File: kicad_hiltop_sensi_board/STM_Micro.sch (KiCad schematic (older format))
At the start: 20 parts, among them SW1 SW_Push, U22 STM32F072RBTx, Y2 8MHZ, Y3 ABS25-32.768KHZ-6-T

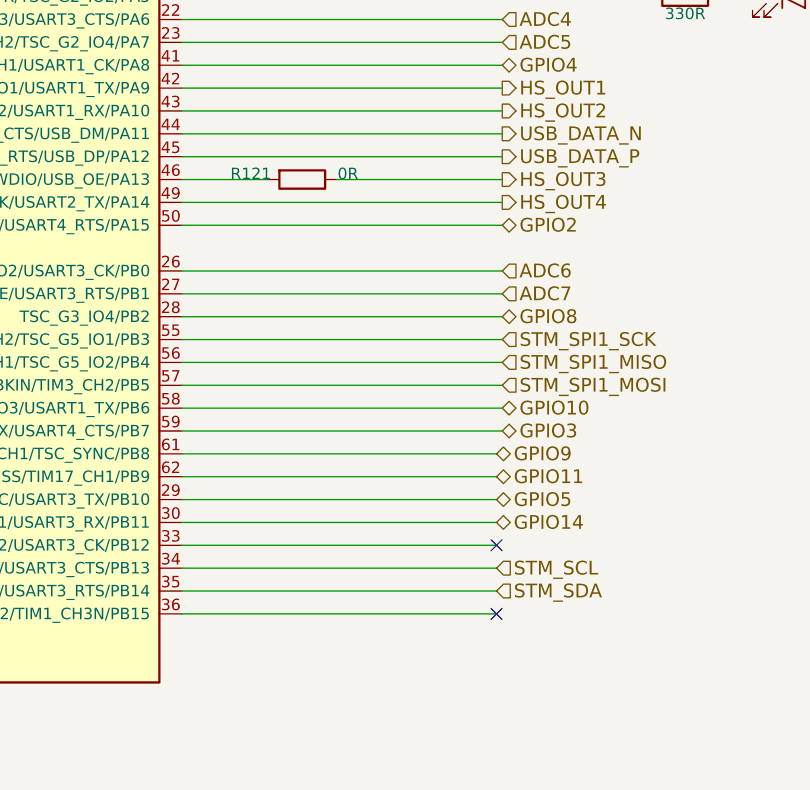
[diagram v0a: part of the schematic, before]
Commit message: Started on Sensi Board Layout
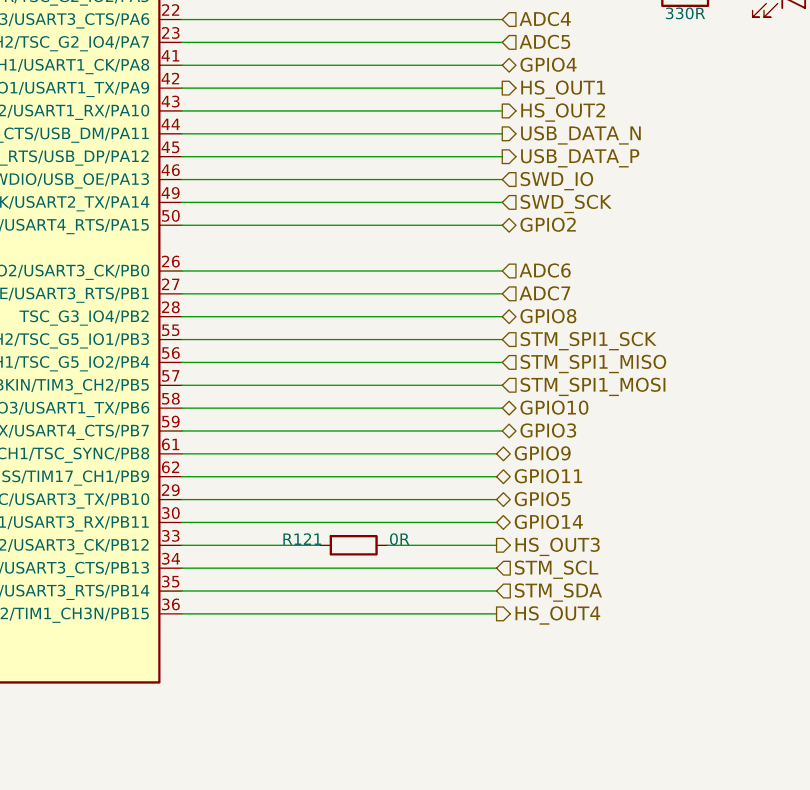
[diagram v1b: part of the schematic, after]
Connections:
- net HS_OUT4: now also U22.36 (I2S2_SD/RTC_REFIN/SPI2_MOSI/SYS_WKUP7/TIM15_CH1N/TIM15_CH2/TIM1_CH3N/PB15); no longer U22.49 (SYS_SWCLK/USART2_TX/PA14)
- net at U22.33 (I2S2_WS/SPI2_NSS/TIM15_BKIN/TIM1_BKIN/TSC_G6_IO2/USART3_CK/PB12): now also R121.2
- net SWD_IO: now reaches U22.46 (IR_OUT/SYS_SWDIO/USB_OE/PA13)
- net SWD_IO: no longer R121.2
- new net SWD_SCK: U22.49 (SYS_SWCLK/USART2_TX/PA14)
- no-connect marks 8 -> 6
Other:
- moved on the sheet: R121
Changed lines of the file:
@@
 	4400 5575 3925 5575
-Wire Wire Line
-	10400 5975 11775 5975
 Wire Wire Line
 	10400 5875 11775 5875
@@
 L Sensi_Board-rescue:R-device R121
 U 1 1 5FA9D488
-P 10925 4375
-F 0 "R121" V 10900 4150 50  0000 C CNN
-F 1 "0R" V 10900 4575 50  0000 C CNN
-F 2 "Resistor_SMD:R_0603_1608Metric" V 10855 4375 50  0001 C CNN
-F 3 "" H 10925 4375 50  0001 C CNN
-F 4 "101-005" H 0   0   50  0001 C CNN "Devtank"
-	1    10925 4375
+P 11150 5975
+F 0 "R121" V 11125 5750 50  0000 C CNN
+F 1 "0R" V 11125 6175 50  0000 C CNN
+F 2 "Resistor_SMD:R_0603_1608Metric" V 11080 5975 50  0001 C CNN
+F 3 "" H 11150 5975 50  0001 C CNN
+F 4 "101-005" H 225 1600 50  0001 C CNN "Devtank"
+	1    11150 5975
 	0    1    1    0
 $EndComp
-Wire Wire Line
-	10775 4375 10400 4375
-Wire Wire Line
-	11075 4375 11800 4375
-Wire Wire Line
-	10400 4475 11800 4475
 Text HLabel 11800 3975 2    60   Output ~ 0
 HS_OUT1
 Text HLabel 11800 4075 2    60   Output ~ 0
 HS_OUT2
-Text HLabel 11800 4375 2    60   Output ~ 0
+Text HLabel 11775 5975 2    60   Output ~ 0
 HS_OUT3
-Text HLabel 11800 4475 2    60   Output ~ 0
+Text HLabel 11775 6275 2    60   Output ~ 0
 HS_OUT4
 Text HLabel 11800 3075 2    60   Input ~ 0
@@
 Text HLabel 11775 6175 2    60   Input ~ 0
 STM_SDA
-NoConn ~ 11775 5975
-NoConn ~ 11775 6275
 NoConn ~ 4400 5375
 NoConn ~ 4400 3475
@@
 Text HLabel 11800 3675 2    60   Input ~ 0
 ADC4
+Wire Wire Line
+	10400 4475 11800 4475
+Wire Wire Line
+	10400 4375 11800 4375
+Text HLabel 11800 4375 2    60   Input ~ 0
+SWD_IO
+Text HLabel 11800 4475 2    60   Input ~ 0
+SWD_SCK
+Wire Wire Line
+	11300 5975 11775 5975
+Wire Wire Line
+	11000 5975 10400 5975
 $EndSCHEMATC

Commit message: Updated sensi board layout LBBC
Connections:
- net ADC1: now also U22.11 (PC3/ADC_IN13/I2S2_SD/SPI2_MOSI); no longer U22.14 (ADC_IN0/COMP1_INM/COMP1_OUT/RTC_TAMP2/SYS_WKUP1/TIM2_CH1/TIM2_ETR/TSC_G1_IO1/USART2_CTS/USART4_TX/PA0)
- net ADC10: now also U22.22 (ADC_IN6/COMP1_OUT/I2S1_MCK/SPI1_MISO/TIM16_CH1/TIM1_BKIN/TIM3_CH1/TSC_G2_IO3/USART3_CTS/PA6); no longer U22.10 (PC2/ADC_IN12/I2S2_MCK/SPI2_MISO)
- net ADC11: now also U22.23 (ADC_IN7/COMP2_OUT/I2S1_SD/SPI1_MOSI/TIM14_CH1/TIM17_CH1/TIM1_CH1N/TIM3_CH2/TSC_G2_IO4/PA7); no longer U22.11 (PC3/ADC_IN13/I2S2_SD/SPI2_MOSI)
- net ADC2: now also U22.10 (PC2/ADC_IN12/I2S2_MCK/SPI2_MISO); no longer U22.15 (ADC_IN1/COMP1_INP/TIM15_CH1N/TIM2_CH2/TSC_G1_IO2/USART2_DE/USART2_RTS/USART4_RX/PA1)
- net ADC3: now also U22.9 (PC1/ADC_IN11); no longer U22.20 (ADC_IN4/COMP1_INM/COMP2_INM/DAC_OUT1/I2S1_WS/SPI1_NSS/TIM14_CH1/TSC_G2_IO1/USART2_CK/PA4)
- net ADC4: now also U22.8 (PC0/ADC_IN10); no longer U22.22 (ADC_IN6/COMP1_OUT/I2S1_MCK/SPI1_MISO/TIM16_CH1/TIM1_BKIN/TIM3_CH1/TSC_G2_IO3/USART3_CTS/PA6)
- net ADC5: now also U22.14 (ADC_IN0/COMP1_INM/COMP1_OUT/RTC_TAMP2/SYS_WKUP1/TIM2_CH1/TIM2_ETR/TSC_G1_IO1/USART2_CTS/USART4_TX/PA0); no longer U22.23 (ADC_IN7/COMP2_OUT/I2S1_SD/SPI1_MOSI/TIM14_CH1/TIM17_CH1/TIM1_CH1N/TIM3_CH2/TSC_G2_IO4/PA7)
- net ADC6: now also U22.15 (ADC_IN1/COMP1_INP/TIM15_CH1N/TIM2_CH2/TSC_G1_IO2/USART2_DE/USART2_RTS/USART4_RX/PA1); no longer U22.26 (ADC_IN8/TIM1_CH2N/TIM3_CH3/TSC_G3_IO2/USART3_CK/PB0)
- net ADC7: now also U22.16 (ADC_IN2/COMP2_INM/COMP2_OUT/SYS_WKUP4/TIM15_CH1/TIM2_CH3/TSC_G1_IO3/USART2_TX/PA2); no longer U22.27 (ADC_IN9/TIM14_CH1/TIM1_CH3N/TIM3_CH4/TSC_G3_IO3/USART3_DE/USART3_RTS/PB1)
- net ADC8: now also U22.17 (ADC_IN3/COMP2_INP/TIM15_CH2/TIM2_CH4/TSC_G1_IO4/USART2_RX/PA3); no longer U22.8 (PC0/ADC_IN10)
- net ADC9: now also U22.20 (ADC_IN4/COMP1_INM/COMP2_INM/DAC_OUT1/I2S1_WS/SPI1_NSS/TIM14_CH1/TSC_G2_IO1/USART2_CK/PA4); no longer U22.9 (PC1/ADC_IN11)
- net DEBUG_UART_RX: now also U22.30 (I2C2_SDA/TIM2_CH4/TSC_G6_IO1/USART3_RX/PB11); no longer U22.17 (ADC_IN3/COMP2_INP/TIM15_CH2/TIM2_CH4/TSC_G1_IO4/USART2_RX/PA3)
- net DEBUG_UART_TX: now also U22.29 (CEC/I2C2_SCL/I2S2_CK/SPI2_SCK/TIM2_CH3/TSC_SYNC/USART3_TX/PB10); no longer U22.16 (ADC_IN2/COMP2_INM/COMP2_OUT/SYS_WKUP4/TIM15_CH1/TIM2_CH3/TSC_G1_IO3/USART2_TX/PA2)
- net DUT1_UART_RX_GPIO15: now also U22.52 (PC11/USART3_RX/USART4_RX); no longer U22.51 (PC10/USART3_TX/USART4_TX)
- net DUT1_UART_TX_GPIO16: now also U22.53 (PC12/USART3_CK/USART4_CK); no longer U22.52 (PC11/USART3_RX/USART4_RX)
- net GPIO1: now also U22.39 (PC8/TIM3_CH3); no longer U22.53 (PC12/USART3_CK/USART4_CK)
- net GPIO10: now also U22.62 (CAN_TX/DAC_EXTI9/I2C1_SDA/I2S2_WS/IR_OUT/SPI2_NSS/TIM17_CH1/PB9); no longer U22.58 (I2C1_SCL/TIM16_CH1N/TSC_G5_IO3/USART1_TX/PB6)
- net GPIO11: now also U22.2 (PC13/RTC_OUT_ALARM/RTC_OUT_CALIB/RTC_TAMP1/RTC_TS/SYS_WKUP2); no longer U22.62 (CAN_TX/DAC_EXTI9/I2C1_SDA/I2S2_WS/IR_OUT/SPI2_NSS/TIM17_CH1/PB9)
- net GPIO12: now also U22.27 (ADC_IN9/TIM14_CH1/TIM1_CH3N/TIM3_CH4/TSC_G3_IO3/USART3_DE/USART3_RTS/PB1); no longer U22.38 (PC7/TIM3_CH2)
- net GPIO14: now also U22.26 (ADC_IN8/TIM1_CH2N/TIM3_CH3/TSC_G3_IO2/USART3_CK/PB0); no longer U22.30 (I2C2_SDA/TIM2_CH4/TSC_G6_IO1/USART3_RX/PB11)
- net GPIO2: now also U22.41 (CRS_SYNC/RCC_MCO/TIM1_CH1/USART1_CK/PA8); no longer U22.50 (I2S1_WS/SPI1_NSS/TIM2_CH1/TIM2_ETR/USART2_RX/USART4_DE/USART4_RTS/PA15)
- net GPIO3: now also U22.28 (TSC_G3_IO4/PB2); no longer U22.59 (I2C1_SDA/TIM17_CH1N/TSC_G5_IO4/USART1_RX/USART4_CTS/PB7)
- net GPIO4: now also U22.42 (DAC_EXTI9/TIM15_BKIN/TIM1_CH2/TSC_G4_IO1/USART1_TX/PA9); no longer U22.41 (CRS_SYNC/RCC_MCO/TIM1_CH1/USART1_CK/PA8)
- net GPIO5: now also U22.34 (I2C2_SCL/I2S2_CK/SPI2_SCK/TIM1_CH1N/TSC_G6_IO3/USART3_CTS/PB13); no longer U22.29 (CEC/I2C2_SCL/I2S2_CK/SPI2_SCK/TIM2_CH3/TSC_SYNC/USART3_TX/PB10)
- net GPIO6: now also U22.35 (I2C2_SDA/I2S2_MCK/SPI2_MISO/TIM15_CH1/TIM1_CH2N/TSC_G6_IO4/USART3_DE/USART3_RTS/PB14); no longer U22.2 (PC13/RTC_OUT_ALARM/RTC_OUT_CALIB/RTC_TAMP1/RTC_TS/SYS_WKUP2)
- net GPIO7: now also U22.36 (I2S2_SD/RTC_REFIN/SPI2_MOSI/SYS_WKUP7/TIM15_CH1N/TIM15_CH2/TIM1_CH3N/PB15); no longer U22.54 (PD2/TIM3_ETR/USART3_DE/USART3_RTS)
- net GPIO8: now also U22.38 (PC7/TIM3_CH2); no longer U22.28 (TSC_G3_IO4/PB2)
- net HS_OUT1: now also U22.43 (TIM17_BKIN/TIM1_CH3/TSC_G4_IO2/USART1_RX/PA10); no longer U22.42 (DAC_EXTI9/TIM15_BKIN/TIM1_CH2/TSC_G4_IO1/USART1_TX/PA9)
- net HS_OUT2: now also U22.33 (I2S2_WS/SPI2_NSS/TIM15_BKIN/TIM1_BKIN/TSC_G6_IO2/USART3_CK/PB12); no longer U22.43 (TIM17_BKIN/TIM1_CH3/TSC_G4_IO2/USART1_RX/PA10)
- net HS_OUT4: now also U22.50 (I2S1_WS/SPI1_NSS/TIM2_CH1/TIM2_ETR/USART2_RX/USART4_DE/USART4_RTS/PA15); no longer U22.36 (I2S2_SD/RTC_REFIN/SPI2_MOSI/SYS_WKUP7/TIM15_CH1N/TIM15_CH2/TIM1_CH3N/PB15)
- net RL1: now also U22.54 (PD2/TIM3_ETR/USART3_DE/USART3_RTS); no longer U22.39 (PC8/TIM3_CH3)
- net STM_SCL: now also U22.58 (I2C1_SCL/TIM16_CH1N/TSC_G5_IO3/USART1_TX/PB6); no longer U22.34 (I2C2_SCL/I2S2_CK/SPI2_SCK/TIM1_CH1N/TSC_G6_IO3/USART3_CTS/PB13)
- net STM_SDA: now also U22.59 (I2C1_SDA/TIM17_CH1N/TSC_G5_IO4/USART1_RX/USART4_CTS/PB7); no longer U22.35 (I2C2_SDA/I2S2_MCK/SPI2_MISO/TIM15_CH1/TIM1_CH2N/TSC_G6_IO4/USART3_DE/USART3_RTS/PB14)
- net at R121.2: now also U22.51 (PC10/USART3_TX/USART4_TX); no longer U22.33 (I2S2_WS/SPI2_NSS/TIM15_BKIN/TIM1_BKIN/TSC_G6_IO2/USART3_CK/PB12)
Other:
- moved on the sheet: R121
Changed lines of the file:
@@
 	4400 5075 3925 5075
 Wire Wire Line
-	4400 5975 3925 5975
-Wire Wire Line
 	10400 4575 11800 4575
 Wire Wire Line
@@
 Wire Wire Line
 	10400 4075 11800 4075
-$Comp
-L Sensi_Board-rescue:R-device R121
-U 1 1 5FA9D488
-P 11150 5975
-F 0 "R121" V 11125 5750 50  0000 C CNN
-F 1 "0R" V 11125 6175 50  0000 C CNN
-F 2 "Resistor_SMD:R_0603_1608Metric" V 11080 5975 50  0001 C CNN
-F 3 "" H 11150 5975 50  0001 C CNN
-F 4 "101-005" H 225 1600 50  0001 C CNN "Devtank"
-	1    11150 5975
-	0    1    1    0
-$EndComp
-Text HLabel 11800 3975 2    60   Output ~ 0
+Text HLabel 11800 4075 2    60   Output ~ 0
 HS_OUT1
-Text HLabel 11800 4075 2    60   Output ~ 0
-HS_OUT2
-Text HLabel 11775 5975 2    60   Output ~ 0
-HS_OUT3
-Text HLabel 11775 6275 2    60   Output ~ 0
+Text HLabel 11800 4575 2    60   Output ~ 0
 HS_OUT4
-Text HLabel 11800 3075 2    60   Input ~ 0
-ADC1
-Text HLabel 11800 3175 2    60   Input ~ 0
-ADC2
-Text HLabel 11800 3375 2    60   Input ~ 0
-DEBUG_UART_RX
-Text HLabel 11800 3275 2    60   Output ~ 0
+Text HLabel 11775 5775 2    60   Output ~ 0
 DEBUG_UART_TX
-Text HLabel 11800 3475 2    60   Input ~ 0
+Text HLabel 3925 4875 0    60   Input ~ 0
 ADC3
 $Comp
@@
 Wire Wire Line
 	13325 3575 13225 3575
-Text HLabel 11800 3775 2    60   Input ~ 0
-ADC5
-Text HLabel 11800 3875 2    60   BiDi ~ 0
+Text HLabel 11800 3975 2    60   BiDi ~ 0
 GPIO4
 Text HLabel 11800 4175 2    60   Output ~ 0
@@
 Text HLabel 11800 4275 2    60   Output ~ 0
 USB_DATA_P
-Text HLabel 11800 4575 2    60   BiDi ~ 0
+Text HLabel 11800 3875 2    60   BiDi ~ 0
 GPIO2
-Text HLabel 11800 4875 2    60   Input ~ 0
+Text HLabel 11800 3275 2    60   Input ~ 0
 ADC7
 Text HLabel 4400 5675 0    60   BiDi ~ 0
 GPIO13
-Text HLabel 4400 6075 0    60   BiDi ~ 0
-GPIO6
-Text HLabel 11800 5375 2    60   BiDi ~ 0
+Text HLabel 11775 5675 2    60   BiDi ~ 0
 GPIO10
-Text HLabel 11800 5475 2    60   BiDi ~ 0
-GPIO3
-Text HLabel 11775 5775 2    60   BiDi ~ 0
+Text HLabel 11775 6075 2    60   BiDi ~ 0
 GPIO5
 Text HLabel 11775 5575 2    60   BiDi ~ 0
 GPIO9
-Text HLabel 11775 5675 2    60   BiDi ~ 0
+Text HLabel 4400 6075 0    60   BiDi ~ 0
 GPIO11
-Text HLabel 11775 5875 2    60   BiDi ~ 0
+Text HLabel 11800 4775 2    60   BiDi ~ 0
 GPIO14
-Text HLabel 3925 4575 0    60   BiDi ~ 0
+Text HLabel 11775 6275 2    60   BiDi ~ 0
 GPIO7
-Text HLabel 3925 4775 0    60   Input ~ 0
-ADC8
-Text HLabel 3925 4875 0    60   Input ~ 0
-ADC9
-Text HLabel 3925 5075 0    60   Input ~ 0
-ADC11
 Text HLabel 3925 5175 0    60   Input ~ 0
 ADC12
 Text HLabel 3925 5275 0    60   Input ~ 0
 ADC13
-Text HLabel 3925 5475 0    60   BiDi ~ 0
+Text HLabel 11800 4875 2    60   BiDi ~ 0
 GPIO12
-Text HLabel 3925 5575 0    60   Output ~ 0
+Text HLabel 3925 4575 0    60   Output ~ 0
 RL1
-Text HLabel 2200 5775 0    60   BiDi ~ 0
+Text HLabel 2500 5875 0    60   BiDi ~ 0
 DUT1_UART_RX_GPIO15
-Text HLabel 3925 5975 0    60   Input ~ 0
+Text HLabel 3925 5575 0    60   Input ~ 0
 GPIO1
-Text HLabel 11800 4775 2    60   Input ~ 0
+Text HLabel 11800 3175 2    60   Input ~ 0
 ADC6
 Wire Wire Line
@@
 Wire Wire Line
 	10400 3175 11800 3175
-Text HLabel 2200 5875 0    60   BiDi ~ 0
+Text HLabel 2500 5975 0    60   BiDi ~ 0
 DUT1_UART_TX_GPIO16
-Wire Wire Line
-	2200 5775 4400 5775
-Wire Wire Line
-	2200 5875 4400 5875
-Text HLabel 11800 4975 2    60   BiDi ~ 0
+Text HLabel 3925 5475 0    60   BiDi ~ 0
 GPIO8
-Text HLabel 3925 4975 0    60   Input ~ 0
-ADC10
 Wire Wire Line
 	2125 3275 4400 3275
@@
 Text HLabel 11800 5275 2    60   Input ~ 0
 STM_SPI1_MOSI
-Text HLabel 11775 6075 2    60   Input ~ 0
+Text HLabel 11800 5375 2    60   Input ~ 0
 STM_SCL
-Text HLabel 11775 6175 2    60   Input ~ 0
+Text HLabel 11800 5475 2    60   Input ~ 0
 STM_SDA
 NoConn ~ 4400 5375
@@
 NoConn ~ 3425 6550
 NoConn ~ 3025 6550
-Text HLabel 11800 3675 2    60   Input ~ 0
-ADC4
 Wire Wire Line
 	10400 4475 11800 4475
@@
 Text HLabel 11800 4475 2    60   Input ~ 0
 SWD_SCK
-Wire Wire Line
-	11300 5975 11775 5975
-Wire Wire Line
-	11000 5975 10400 5975
+Text HLabel 11800 3475 2    60   Input ~ 0
+ADC9
+Text HLabel 11800 3375 2    60   Input ~ 0
+ADC8
+Text HLabel 3925 4775 0    60   Input ~ 0
+ADC4
+Text HLabel 11800 3075 2    60   Input ~ 0
+ADC5
+Text HLabel 3925 4975 0    60   Input ~ 0
+ADC2
+Text HLabel 3925 5075 0    60   Input ~ 0
+ADC1
+Text HLabel 11800 5975 2    60   Output ~ 0
+HS_OUT2
+Text HLabel 11800 4975 2    60   BiDi ~ 0
+GPIO3
+Text HLabel 11775 6175 2    60   BiDi ~ 0
+GPIO6
+Wire Wire Line
+	3800 5775 4400 5775
+Wire Wire Line
+	3500 5775 3025 5775
+Text HLabel 11775 5875 2    60   Input ~ 0
+DEBUG_UART_RX
+Text HLabel 3025 5775 0    60   Output ~ 0
+HS_OUT3
+$Comp
+L Sensi_Board-rescue:R-device R121
+U 1 1 5FA9D488
+P 3650 5775
+F 0 "R121" V 3625 5550 50  0000 C CNN
+F 1 "0R" V 3625 5975 50  0000 C CNN
+F 2 "Resistor_SMD:R_0603_1608Metric" V 3580 5775 50  0001 C CNN
+F 3 "" H 3650 5775 50  0001 C CNN
+F 4 "101-005" H -7275 1400 50  0001 C CNN "Devtank"
+	1    3650 5775
+	0    -1   1    0
+$EndComp
+Wire Wire Line
+	2500 5875 4400 5875
+Wire Wire Line
+	4400 5975 2500 5975
+Wire Wire Line
+	10400 5975 11800 5975
+Text HLabel 11800 3675 2    60   Input ~ 0
+ADC10
+Text HLabel 11800 3775 2    60   Input ~ 0
+ADC11
 $EndSCHEMATC

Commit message: Sensi board updated pin map
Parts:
- C73, C74, C79, C80: footprint Capacitor_SMD:C_0603_1608Metric -> Capacitor_SMD:C_0402_1005Metric
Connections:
- net ADC1: now also U22.14 (ADC_IN0/COMP1_INM/COMP1_OUT/RTC_TAMP2/SYS_WKUP1/TIM2_CH1/TIM2_ETR/TSC_G1_IO1/USART2_CTS/USART4_TX/PA0); no longer U22.11 (PC3/ADC_IN13/I2S2_SD/SPI2_MOSI)
- net ADC10: now also U22.25 (PC5/ADC_IN15/SYS_WKUP5/TSC_G3_IO1/USART3_RX); no longer U22.22 (ADC_IN6/COMP1_OUT/I2S1_MCK/SPI1_MISO/TIM16_CH1/TIM1_BKIN/TIM3_CH1/TSC_G2_IO3/USART3_CTS/PA6)
- net ADC11: now also U22.24 (PC4/ADC_IN14/USART3_TX); no longer U22.23 (ADC_IN7/COMP2_OUT/I2S1_SD/SPI1_MOSI/TIM14_CH1/TIM17_CH1/TIM1_CH1N/TIM3_CH2/TSC_G2_IO4/PA7)
- net ADC12: now also U22.23 (ADC_IN7/COMP2_OUT/I2S1_SD/SPI1_MOSI/TIM14_CH1/TIM17_CH1/TIM1_CH1N/TIM3_CH2/TSC_G2_IO4/PA7); no longer U22.24 (PC4/ADC_IN14/USART3_TX)
- net ADC13: now also U22.8 (PC0/ADC_IN10); no longer U22.25 (PC5/ADC_IN15/SYS_WKUP5/TSC_G3_IO1/USART3_RX)
- net ADC2: now also U22.11 (PC3/ADC_IN13/I2S2_SD/SPI2_MOSI); no longer U22.10 (PC2/ADC_IN12/I2S2_MCK/SPI2_MISO)
- net ADC3: now also U22.10 (PC2/ADC_IN12/I2S2_MCK/SPI2_MISO); no longer U22.9 (PC1/ADC_IN11)
- net ADC4: now also U22.9 (PC1/ADC_IN11); no longer U22.8 (PC0/ADC_IN10)
- net ADC5: now also U22.16 (ADC_IN2/COMP2_INM/COMP2_OUT/SYS_WKUP4/TIM15_CH1/TIM2_CH3/TSC_G1_IO3/USART2_TX/PA2); no longer U22.14 (ADC_IN0/COMP1_INM/COMP1_OUT/RTC_TAMP2/SYS_WKUP1/TIM2_CH1/TIM2_ETR/TSC_G1_IO1/USART2_CTS/USART4_TX/PA0)
- net ADC6: now also U22.17 (ADC_IN3/COMP2_INP/TIM15_CH2/TIM2_CH4/TSC_G1_IO4/USART2_RX/PA3); no longer U22.15 (ADC_IN1/COMP1_INP/TIM15_CH1N/TIM2_CH2/TSC_G1_IO2/USART2_DE/USART2_RTS/USART4_RX/PA1)
- net ADC7: now also U22.20 (ADC_IN4/COMP1_INM/COMP2_INM/DAC_OUT1/I2S1_WS/SPI1_NSS/TIM14_CH1/TSC_G2_IO1/USART2_CK/PA4); no longer U22.16 (ADC_IN2/COMP2_INM/COMP2_OUT/SYS_WKUP4/TIM15_CH1/TIM2_CH3/TSC_G1_IO3/USART2_TX/PA2)
- net ADC8: now also U22.22 (ADC_IN6/COMP1_OUT/I2S1_MCK/SPI1_MISO/TIM16_CH1/TIM1_BKIN/TIM3_CH1/TSC_G2_IO3/USART3_CTS/PA6); no longer U22.17 (ADC_IN3/COMP2_INP/TIM15_CH2/TIM2_CH4/TSC_G1_IO4/USART2_RX/PA3)
- net ADC9: now also U22.27 (ADC_IN9/TIM14_CH1/TIM1_CH3N/TIM3_CH4/TSC_G3_IO3/USART3_DE/USART3_RTS/PB1); no longer U22.20 (ADC_IN4/COMP1_INM/COMP2_INM/DAC_OUT1/I2S1_WS/SPI1_NSS/TIM14_CH1/TSC_G2_IO1/USART2_CK/PA4)
- net GPIO10: now also U22.61 (CAN_RX/CEC/I2C1_SCL/TIM16_CH1/TSC_SYNC/PB8); no longer U22.62 (CAN_TX/DAC_EXTI9/I2C1_SDA/I2S2_WS/IR_OUT/SPI2_NSS/TIM17_CH1/PB9)
- net GPIO12: now also U22.15 (ADC_IN1/COMP1_INP/TIM15_CH1N/TIM2_CH2/TSC_G1_IO2/USART2_DE/USART2_RTS/USART4_RX/PA1); no longer U22.27 (ADC_IN9/TIM14_CH1/TIM1_CH3N/TIM3_CH4/TSC_G3_IO3/USART3_DE/USART3_RTS/PB1)
- net GPIO9: now also U22.54 (PD2/TIM3_ETR/USART3_DE/USART3_RTS); no longer U22.61 (CAN_RX/CEC/I2C1_SCL/TIM16_CH1/TSC_SYNC/PB8)
- net RL1: now also U22.62 (CAN_TX/DAC_EXTI9/I2C1_SDA/I2S2_WS/IR_OUT/SPI2_NSS/TIM17_CH1/PB9); no longer U22.54 (PD2/TIM3_ETR/USART3_DE/USART3_RTS)
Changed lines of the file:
@@
 $EndComp
-Wire Wire Line
-	7500 1725 7500 1775
 Wire Wire Line
 	7200 2575 7200 1825
@@
 F 0 "C73" H 2240 1671 50  0000 L CNN
 F 1 "100nF" H 2240 1580 50  0000 L CNN
-F 2 "Capacitor_SMD:C_0603_1608Metric" H 2163 1475 50  0001 C CNN
+F 2 "Capacitor_SMD:C_0402_1005Metric" H 2163 1475 50  0001 C CNN
 F 3 "" H 2125 1625 50  0001 C CNN
 F 4 "105-002" H 0   0   50  0001 C CNN "Devtank"
@@
 F 0 "C74" H 2690 1671 50  0000 L CNN
 F 1 "100nF" H 2690 1580 50  0000 L CNN
-F 2 "Capacitor_SMD:C_0603_1608Metric" H 2613 1475 50  0001 C CNN
+F 2 "Capacitor_SMD:C_0402_1005Metric" H 2613 1475 50  0001 C CNN
 F 3 "" H 2575 1625 50  0001 C CNN
 F 4 "105-002" H 0   0   50  0001 C CNN "Devtank"
@@
 F 0 "C79" H 3140 1671 50  0000 L CNN
 F 1 "100nF" H 3140 1580 50  0000 L CNN
-F 2 "Capacitor_SMD:C_0603_1608Metric" H 3063 1475 50  0001 C CNN
+F 2 "Capacitor_SMD:C_0402_1005Metric" H 3063 1475 50  0001 C CNN
 F 3 "" H 3025 1625 50  0001 C CNN
 F 4 "105-002" H 0   0   50  0001 C CNN "Devtank"
@@
 F 0 "C80" H 3590 1671 50  0000 L CNN
 F 1 "100nF" H 3590 1580 50  0000 L CNN
-F 2 "Capacitor_SMD:C_0603_1608Metric" H 3513 1475 50  0001 C CNN
+F 2 "Capacitor_SMD:C_0402_1005Metric" H 3513 1475 50  0001 C CNN
 F 3 "" H 3475 1625 50  0001 C CNN
 F 4 "105-002" H 0   0   50  0001 C CNN "Devtank"
@@
 Text HLabel 11775 5775 2    60   Output ~ 0
 DEBUG_UART_TX
-Text HLabel 3925 4875 0    60   Input ~ 0
+Text HLabel 3925 4975 0    60   Input ~ 0
 ADC3
 $Comp
@@
 Text HLabel 11800 3875 2    60   BiDi ~ 0
 GPIO2
-Text HLabel 11800 3275 2    60   Input ~ 0
+Text HLabel 11800 3475 2    60   Input ~ 0
 ADC7
 Text HLabel 4400 5675 0    60   BiDi ~ 0
 GPIO13
-Text HLabel 11775 5675 2    60   BiDi ~ 0
+Text HLabel 11775 5575 2    60   BiDi ~ 0
 GPIO10
 Text HLabel 11775 6075 2    60   BiDi ~ 0
 GPIO5
-Text HLabel 11775 5575 2    60   BiDi ~ 0
+Text HLabel 3925 4575 0    60   BiDi ~ 0
 GPIO9
 Text HLabel 4400 6075 0    60   BiDi ~ 0
@@
 Text HLabel 11775 6275 2    60   BiDi ~ 0
 GPIO7
-Text HLabel 3925 5175 0    60   Input ~ 0
+Text HLabel 11800 3775 2    60   Input ~ 0
 ADC12
-Text HLabel 3925 5275 0    60   Input ~ 0
+Text HLabel 3925 4775 0    60   Input ~ 0
 ADC13
-Text HLabel 11800 4875 2    60   BiDi ~ 0
+Text HLabel 11800 3175 2    60   BiDi ~ 0
 GPIO12
-Text HLabel 3925 4575 0    60   Output ~ 0
+Text HLabel 11775 5675 2    60   Output ~ 0
 RL1
 Text HLabel 2500 5875 0    60   BiDi ~ 0
@@
 Text HLabel 3925 5575 0    60   Input ~ 0
 GPIO1
-Text HLabel 11800 3175 2    60   Input ~ 0
+Text HLabel 11800 3375 2    60   Input ~ 0
 ADC6
 Wire Wire Line
@@
 NoConn ~ 4400 5375
 NoConn ~ 4400 3475
-$Comp
-L power:PWR_FLAG #FLG0102
-U 1 1 5E858D18
-P 7375 1725
-F 0 "#FLG0102" H 7375 1800 50  0001 C CNN
-F 1 "PWR_FLAG" H 7375 1898 50  0000 C CNN
-F 2 "" H 7375 1725 50  0001 C CNN
-F 3 "" H 7375 1725 50  0001 C CNN
-	1    7375 1725
-	1    0    0    -1
-$EndComp
-Wire Wire Line
-	7375 1725 7375 1775
-Wire Wire Line
-	7375 1775 7500 1775
-Connection ~ 7500 1775
-Wire Wire Line
-	7500 1775 7500 1825
 NoConn ~ 3250 4325
 NoConn ~ 2850 4325
@@
 Text HLabel 11800 4475 2    60   Input ~ 0
 SWD_SCK
-Text HLabel 11800 3475 2    60   Input ~ 0
+Text HLabel 11800 4875 2    60   Input ~ 0
 ADC9
-Text HLabel 11800 3375 2    60   Input ~ 0
+Text HLabel 11800 3675 2    60   Input ~ 0
 ADC8
-Text HLabel 3925 4775 0    60   Input ~ 0
+Text HLabel 3925 4875 0    60   Input ~ 0
 ADC4
+Text HLabel 11800 3275 2    60   Input ~ 0
+ADC5
+Text HLabel 3925 5075 0    60   Input ~ 0
+ADC2
 Text HLabel 11800 3075 2    60   Input ~ 0
-ADC5
-Text HLabel 3925 4975 0    60   Input ~ 0
-ADC2
-Text HLabel 3925 5075 0    60   Input ~ 0
 ADC1
 Text HLabel 11800 5975 2    60   Output ~ 0
@@
 Wire Wire Line
 	10400 5975 11800 5975
-Text HLabel 11800 3675 2    60   Input ~ 0
+Text HLabel 3925 5275 0    60   Input ~ 0
 ADC10
-Text HLabel 11800 3775 2    60   Input ~ 0
+Text HLabel 3925 5175 0    60   Input ~ 0
 ADC11
+Wire Wire Line
+	7500 1725 7500 1825
 $EndSCHEMATC
